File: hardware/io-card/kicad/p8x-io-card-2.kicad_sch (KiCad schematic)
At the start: 9 parts, among them U10 74HCT374, U11 74HCT244, U12 74HCT244, U13 74HCT244, U14 6850, U15 74HCT00, U16 DS1302, U17 6850, U18 74HCT14

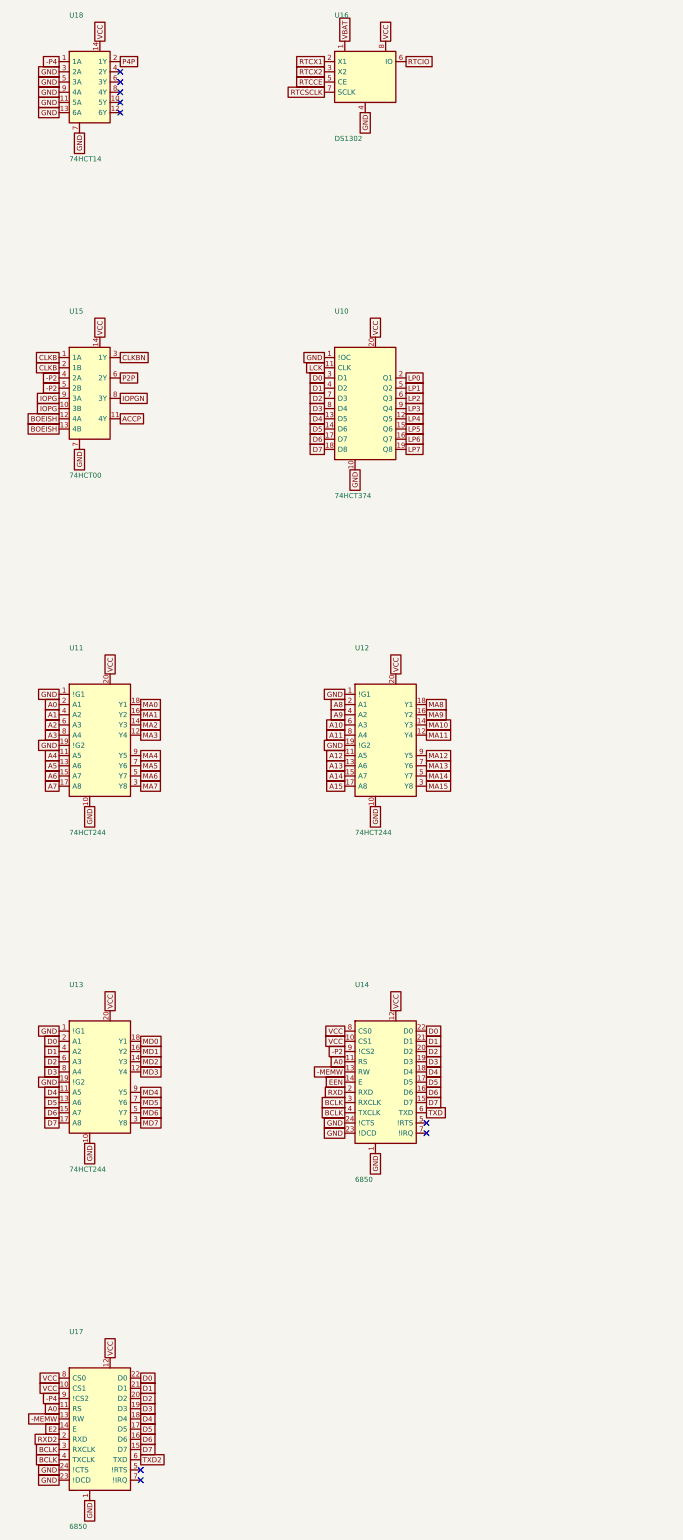
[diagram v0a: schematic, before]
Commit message: feat(sch): draw the io-card schematic by function
Group the io-card into functional sheets (address decode, switch/LED
ports, serial, bus monitor, RTC) with each block's resistors, LEDs,
crystals and connectors on the same sheet, so local nets are drawn as
wires: 18 -> ~330 wires. Orient wires by drawing side on this card
(FLOW_BY_SIDE) so the ACIA -> MAX232 round trip lays out left to right;
put the 6850 and MAX232 bus/TTL pins left and serial/RS-232 pins right;
draw the RX/TX swap jumpers with a schematic-only JMP2X3SWAP variant.
Netlist still matches the board (155 nets, 562 pins), ERC 0 errors.

Co-Authored-By: Claude Opus 5.5 <noreply@anthropic.com>
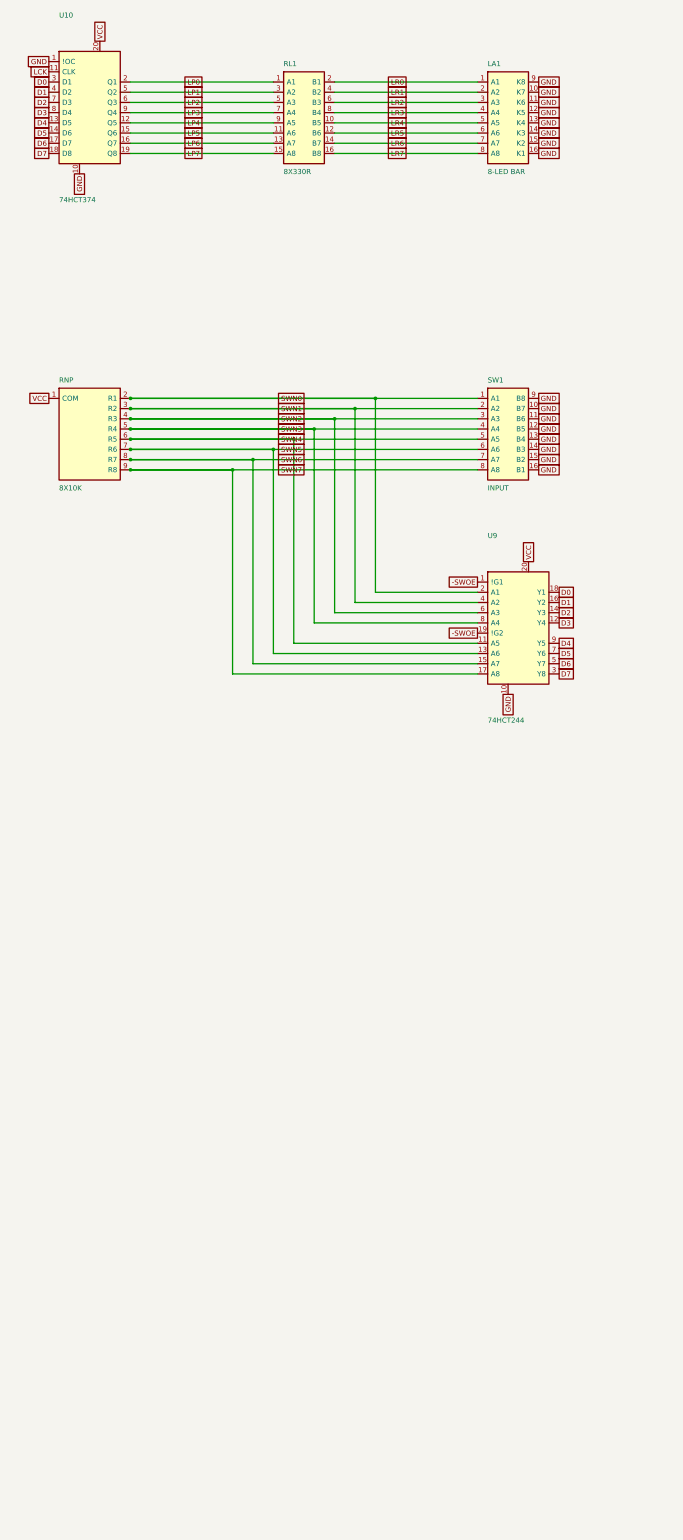
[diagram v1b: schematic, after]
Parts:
- removed U11, U12, U13: 74HCT244, Package_DIP:DIP-20_W7.62mm, symbol p8x:74244
- removed U14, U17: 6850, Package_DIP:DIP-24_W15.24mm, symbol p8x:6850
- removed U15: 74HCT00, Package_DIP:DIP-14_W7.62mm, symbol p8x:GATES14
- removed U16: DS1302, Package_DIP:DIP-8_W7.62mm, symbol p8x:DS1302
- removed U18: 74HCT14, Package_DIP:DIP-14_W7.62mm, symbol p8x:HEX14
- added LA1: 8-LED BAR, Package_DIP:DIP-16_W7.62mm, symbol p8x:LEDARR8
- added RL1: 8X330R, Connector_PinHeader_2.54mm:PinHeader_1x16_P2.54mm_Vertical, symbol p8x:RNISO8
- added RNP: 8X10K, Resistor_THT:R_Array_SIP9, symbol p8x:SIP9
- added SW1: INPUT, Button_Switch_THT:SW_DIP_SPSTx08_Slide_9.78x22.5mm_W7.62mm_P2.54mm, symbol p8x:DIP8SW
- added U9: 74HCT244, Package_DIP:DIP-20_W7.62mm, symbol p8x:74244
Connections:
- net D0: now also U9.18 (Y1)
- net D1: now also U9.16 (Y2)
- net D2: now also U9.14 (Y3)
- net D3: now also U9.12 (Y4)
- net D4: now also U9.9 (Y5)
- net D5: now also U9.7 (Y6)
- net D6: now also U9.5 (Y7)
- net D7: now also U9.3 (Y8)
- net GND: now also LA1.10 (K7), LA1.11 (K6), LA1.12 (K5), LA1.13 (K4), LA1.14 (K3), LA1.15 (K2), LA1.16 (K1), LA1.9 (K8), SW1.10 (B7), SW1.11 (B6), SW1.12 (B5), SW1.13 (B4), SW1.14 (B3), SW1.15 (B2), SW1.16 (B1), SW1.9 (B8), U9.10
- net LP0: now also RL1.1 (A1)
- net LP1: now also RL1.3 (A2)
- net LP2: now also RL1.5 (A3)
- net LP3: now also RL1.7 (A4)
- net LP4: now also RL1.9 (A5)
- net LP5: now also RL1.11 (A6)
- net LP6: now also RL1.13 (A7)
- net LP7: now also RL1.15 (A8)
- net VCC: now also RNP.1 (COM), U9.20
- new net -SWOE: U9.1 (!G1), U9.19 (!G2)
- new net LR0: LA1.1 (A1), RL1.2 (B1)
- new net LR1: LA1.2 (A2), RL1.4 (B2)
- new net LR2: LA1.3 (A3), RL1.6 (B3)
- new net LR3: LA1.4 (A4), RL1.8 (B4)
- new net LR4: LA1.5 (A5), RL1.10 (B5)
- new net LR5: LA1.6 (A6), RL1.12 (B6)
- new net LR6: LA1.7 (A7), RL1.14 (B7)
- new net LR7: LA1.8 (A8), RL1.16 (B8)
- new net SWN0: RNP.2 (R1), SW1.1 (A1), U9.2 (A1)
- new net SWN1: RNP.3 (R2), SW1.2 (A2), U9.4 (A2)
- new net SWN2: RNP.4 (R3), SW1.3 (A3), U9.6 (A3)
- new net SWN3: RNP.5 (R4), SW1.4 (A4), U9.8 (A4)
- new net SWN4: RNP.6 (R5), SW1.5 (A5), U9.11 (A5)
- new net SWN5: RNP.7 (R6), SW1.6 (A6), U9.13 (A6)
- new net SWN6: RNP.8 (R7), SW1.7 (A7), U9.15 (A7)
- new net SWN7: RNP.9 (R8), SW1.8 (A8), U9.17 (A8)
- no-connect marks 9 -> 0
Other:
- moved on the sheet: U10

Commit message: feat(sch): draw every P8X card schematic by function
Extend the functional-sheet grouping from the io-card to the control,
regbank, alu, memory, cf, ps2 and bustest cards. functional_sheets now
attaches unnamed glue gates, LEDs, resistors and connectors to the block
they share the most local nets with, so each block lists only its main
parts. A net with two or more pins on a sheet is now wired there even if
it continues elsewhere (its global name label rides on the wire), and
every wire is oriented by drawing side. The regbank gets one pointer per
sheet; the ps2 latches share a sheet with the AVR so the mailbox bus is
drawn. The bustest probe resistors use a straight-order RNISO8DSTR
drawing (the reversed B side forced every wire to cross and the sheet
fell back to labels). build_sch.sh now shows ELK fallbacks and clears old
numbered sheets before a build. All eight netlists match the boards,
ERC 0 errors; the boards change only in footprint link paths.

Co-Authored-By: Claude Opus 5.5 <noreply@anthropic.com>
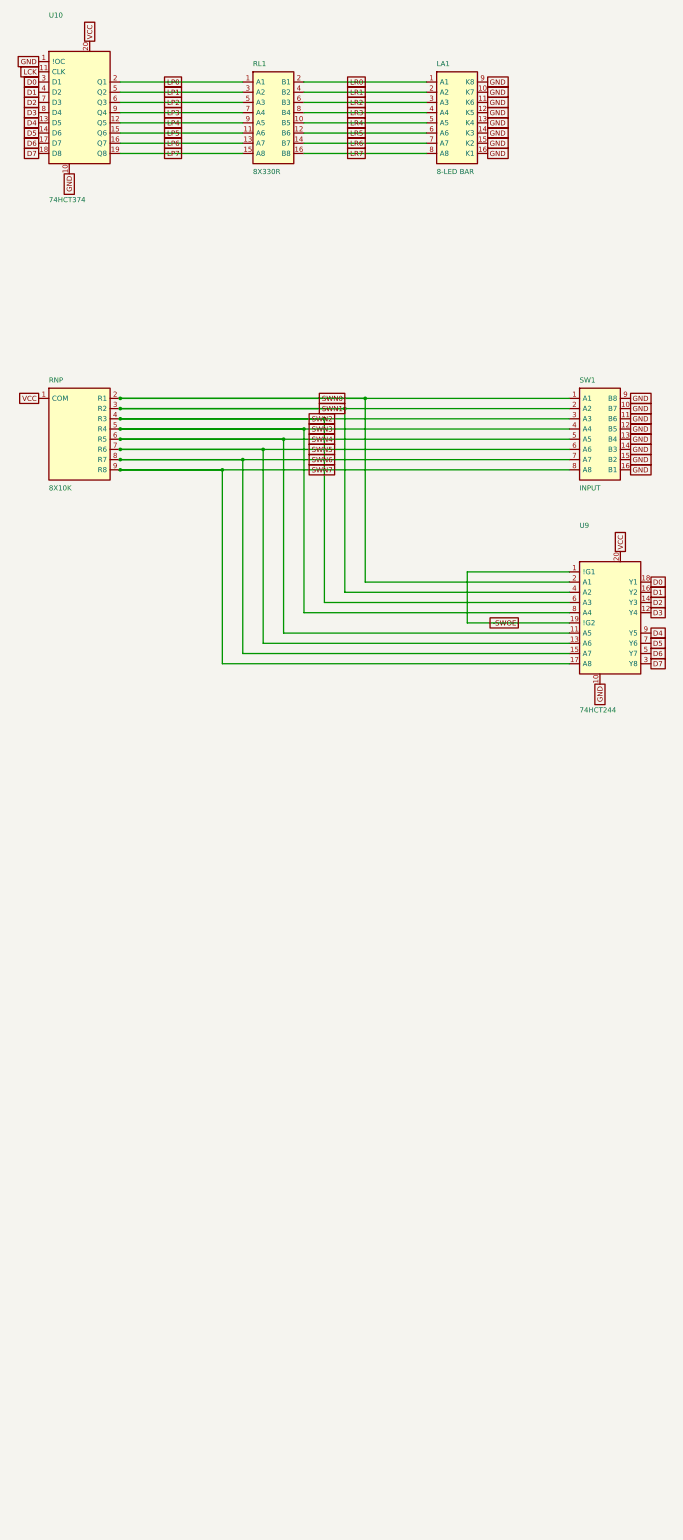
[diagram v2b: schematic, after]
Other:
- moved on the sheet: LA1, RL1, RNP, SW1, U10, U9

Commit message: fix(io): isolated LED resistor banks as DIP-16 networks
RL1 and RM1-RM3 were RNISO8 on a 1x16 pin-header footprint; no
16-pin isolated SIP exists, and the render showed a header. Switch to
RNISO8D (DIP-16), per the WONT-DO resistor packaging rule and matching
the bus test card. Place each network beside its bargraph so pins
16-9 face the anodes straight across; draw them with the straight
RNISO8DSTR schematic variant; BOM names the DIP-16 part and is
regenerated (it was months stale). io-card re-routed: PASS.

Co-Authored-By: Claude Opus 5.5 <noreply@anthropic.com>
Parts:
- RL1: footprint Connector_PinHeader_2.54mm:PinHeader_1x16_P2.54mm_Vertical -> Package_DIP:DIP-16_W7.62mm; symbol p8x:RNISO8 -> p8x:RNISO8DSTR
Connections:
- net LP1: now also RL1.2 (A2); no longer RL1.3 (A2)
- net LP2: now also RL1.3 (A3); no longer RL1.5 (A3)
- net LP3: now also RL1.4 (A4); no longer RL1.7 (A4)
- net LP4: now also RL1.5 (A5); no longer RL1.9 (A5)
- net LP5: now also RL1.6 (A6); no longer RL1.11 (A6)
- net LP6: now also RL1.7 (A7); no longer RL1.13 (A7)
- net LP7: now also RL1.8 (A8); no longer RL1.15 (A8)
- net LR0: now also RL1.16 (B1); no longer RL1.2 (B1)
- net LR1: now also RL1.15 (B2); no longer RL1.4 (B2)
- net LR2: now also RL1.14 (B3); no longer RL1.6 (B3)
- net LR3: now also RL1.13 (B4); no longer RL1.8 (B4)
- net LR4: now also RL1.12 (B5); no longer RL1.10 (B5)
- net LR5: now also RL1.11 (B6); no longer RL1.12 (B6)
- net LR6: now also RL1.10 (B7); no longer RL1.14 (B7)
- net LR7: now also RL1.9 (B8); no longer RL1.16 (B8)
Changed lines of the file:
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@@
   (global_label "VCC" (shape passive) (at 68.58 50.80 90) (fields_autoplaced yes) (effects (font (size 1.27 1.27)) (justify left))
     (property "Intersheetrefs" "${INTERSHEET_REFS}" (at 68.58 50.80 0) (effects (font (size 1.27 1.27)) hide)))
-  (symbol (lib_id "p8x:RNISO8") (at 114.30 71.12 0) (unit 1) (in_bom yes) (on_board yes) (dnp no)
+  (symbol (lib_id "p8x:RNISO8DSTR") (at 114.30 71.12 0) (unit 1) (in_bom yes) (on_board yes) (dnp no)
     (property "Reference" "RL1" (at 109.22 56.42 0) (effects (font (size 1.27 1.27)) (justify left)))
     (property "Value" "8X330R" (at 109.22 83.28 0) (effects (font (size 1.27 1.27)) (justify left)))
-    (property "Footprint" "Connector_PinHeader_2.54mm:PinHeader_1x16_P2.54mm_Vertical" (at 114.30 71.12 0) (effects (font (size 1.27 1.27)) hide))
+    (property "Footprint" "Package_DIP:DIP-16_W7.62mm" (at 114.30 71.12 0) (effects (font (size 1.27 1.27)) hide))
     (property "Datasheet" "" (at 114.30 71.12 0) (effects (font (size 1.27 1.27)) hide))
     (pin "1")
+    (pin "2")
     (pin "3")
+    (pin "4")
     (pin "5")
+    (pin "6")
     (pin "7")
+    (pin "8")
+    (pin "16")
+    (pin "15")
+    (pin "14")
+    (pin "13")
+    (pin "12")
+    (pin "11")
+    (pin "10")
     (pin "9")
-    (pin "11")
-    (pin "13")
-    (pin "15")
-    (pin "2")
-    (pin "4")
-    (pin "6")
-    (pin "8")
-    (pin "10")
-    (pin "12")
-    (pin "14")
-    (pin "16")
     (instances (project "p8x-io-card" (path "/ed807a3d-9122-5982-9811-120926e12b80/c7bdcd3f-ad79-5999-93b4-87ed80ac18da" (reference "RL1") (unit 1))))
   )
